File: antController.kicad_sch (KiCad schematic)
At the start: 79 parts

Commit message: work on schematic
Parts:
- removed J?: Proto_matrix, Critbit_lib:Proto_matrix_14x10, symbol Critbit_lib:Proto_matrix
- removed J?: DISP_OLED, symbol Connector_Generic:Conn_01x04
- removed J?: MOSFET_SINKS, symbol Connector:Screw_Terminal_01x16
- removed J?: OC_2, symbol Connector:Screw_Terminal_01x16
- removed JP?: 5V_SEL, symbol Jumper:SolderJumper_3_Open
- removed R? (x2): 4k7, Resistor_SMD:R_0603_1608Metric_Pad1.05x0.95mm_HandSolder, symbol Device:R
- removed R? (x2): 200, Resistor_SMD:R_0603_1608Metric_Pad1.05x0.95mm_HandSolder, symbol Device:R
- removed R? (x4): 1k, Resistor_SMD:R_0603_1608Metric_Pad1.05x0.95mm_HandSolder, symbol Device:R
- removed U?: 74LS540, symbol 74xx:74LS540
- added C? (x3): 100n, Capacitor_SMD:C_0603_1608Metric_Pad1.05x0.95mm_HandSolder, symbol Device:C_Small
- added D?: LED_RED, LED_SMD:LED_0805_2012Metric_Pad1.15x1.40mm_HandSolder, symbol Device:LED
- added J?: IO_OUT, symbol Connector_Generic:Conn_01x07
- added J? (x2): Screw_Terminal_01x20, symbol Connector:Screw_Terminal_01x20
- added J? (x3): IN_1, symbol Connector:Screw_Terminal_01x05
- added JP?: IOEX_A2_SEL, symbol Jumper:SolderJumper_3_Open
- added K?: AZ850-x, Relay_THT:Relay_DPDT_FRT5, symbol Relay:AZ850-x
- added Q? (x2): MMBT2222A, Package_TO_SOT_SMD:SOT-23, symbol Device:Q_NPN_BEC
- added R? (x7): 10k, Resistor_SMD:R_0603_1608Metric_Pad1.05x0.95mm_HandSolder, symbol Device:R
- added R? (x5): 4k7, Resistor_SMD:R_0603_1608Metric_Pad1.05x0.95mm_HandSolder, symbol Device:R
- added R?: 200k, Resistor_SMD:R_0603_1608Metric_Pad1.05x0.95mm_HandSolder, symbol Device:R
- added U? (x3): 74HC244, symbol 74xx:74HC244
- added U?: PCA9306DC, Package_SO:VSSOP-8_2.3x2mm_P0.5mm, symbol Interface:PCA9306DC
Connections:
- net +3.3V: now also C?.1, J?.2 (Pin_2), R?.2, R?.2, U?.2 (VREF1)
- net +3V3: now also C?.1, C?.1, U?.20 (VCC), U?.20 (VCC)
- net +5V: now also J?.1 (Pin_1), JP?.3 (B), K?.1, Q?.1 (B), R?.2, U?.20 (VCC)
- net BUFF1: now also J?.5 (Pin_5), U?.18 (1Y0)
- net BUFF2: now also J?.6 (Pin_6), U?.16 (1Y1)
- net BUFF3: now also J?.7 (Pin_7), U?.14 (1Y2)
- net BUFF4: now also J?.8 (Pin_8), U?.12 (1Y3)
- net BUFF5: now also J?.9 (Pin_9), U?.3 (2Y0)
- net BUFF6: now also J?.10 (Pin_10), U?.5 (2Y1)
- net BUFF7: now also J?.11 (Pin_11), U?.7 (2Y2)
- net BUFF8: now also J?.12 (Pin_12), U?.9 (2Y3)
- net GND: now also U?.2, C?.2, C?.2, C?.2, J?.13 (Pin_13), J?.19 (Pin_19), J?.2 (Pin_2), J?.20 (Pin_20), J?.3 (Pin_3), J?.4 (Pin_4), J?.5 (Pin_5), J?.5 (Pin_5), J?.5 (Pin_5), J?.7 (Pin_7), JP?.1 (A), Q?.2 (E), R?.1, R?.1, R?.1, R?.1, R?.1, R?.1, U?.1 (GND), U?.10 (GND), U?.10 (GND), U?.10 (GND); no longer R?.1, U?.3 (A2), U?.3 (A2), U?.3 (A2)
- net G_SINK1: now also R?.2; no longer Q?.1 (G)
- net IO14: now also U?.18 (1Y0)
- net IO15: now also U?.16 (1Y1)
- net IO16: now also U?.14 (1Y2)
- net IO17: now also U?.12 (1Y3)
- net IO18: now also U?.3 (2Y0)
- net IO19: now also U?.5 (2Y1)
- net IO21: now also U?.7 (2Y2)
- net IO22: now also U?.9 (2Y3)
- net IO23: now also U?.18 (1Y0)
- net IO25: now also U?.16 (1Y1)
- net IO26: now also U?.14 (1Y2)
- net IO27: now also U?.12 (1Y3)
- net IO32: now also J?.5 (Pin_5)
- net IO33: now also J?.6 (Pin_6)
- net OC1_A: now also R?.2; no longer U?.1
- net SINK1: now also J?.3 (Pin_3)
- net SINK10: now also J?.12 (Pin_12)
- net SINK11: now also J?.13 (Pin_13)
- net SINK12: now also J?.14 (Pin_14)
- net SINK13: now also J?.15 (Pin_15)
- net SINK14: now also J?.16 (Pin_16)
- net SINK15: now also J?.17 (Pin_17)
- net SINK16: now also J?.18 (Pin_18)
- net SINK2: now also J?.4 (Pin_4)
- net SINK3: now also J?.5 (Pin_5)
- net SINK4: now also J?.6 (Pin_6)
- net SINK5: now also J?.7 (Pin_7)
- net SINK6: now also J?.8 (Pin_8)
- net SINK7: now also J?.9 (Pin_9)
- net SINK8: now also J?.10 (Pin_10)
- net SINK9: now also J?.11 (Pin_11)
- net at U?.10 (IO0_6): now also U?.13 (2A2)
- net at U?.11 (IO0_7): now also U?.11 (2A3)
- net OUT_BUFF_ENA: now reaches R?.2, U?.13 (IO1_0)
- net OUT_BUFF_ENA: now also U?.1 (1OE), U?.19 (2OE)
- net IN_BUFF_ENA: now reaches U?.14 (IO1_1)
- net IN_BUFF_ENA: now also U?.1 (1OE), U?.1 (1OE), U?.19 (2OE), U?.19 (2OE)
- net at U?.18 (IO1_5): now also R?.2
- net LED1: now reaches U?.19 (IO1_6)
- net LED1: now also R?.1
- net LED2: now reaches U?.20 (IO1_7)
- net LED2: now also R?.1
- net at U?.4 (IO0_0): now also U?.2 (1A0)
- net at U?.5 (IO0_1): now also U?.4 (1A1)
- net at U?.6 (IO0_2): now also U?.6 (1A2)
- net at U?.7 (IO0_3): now also U?.8 (1A3)
- net at U?.8 (IO0_4): now also U?.17 (2A0)
- net at U?.9 (IO0_5): now also U?.15 (2A1)
- net at D?.1 (K): now also R?.2 (x6)
- net DISP_SCL: no longer names the net of U?.14 (IO12)
- net DISP_SCL: now also J?.3 (Pin_3); no longer J?.1 (Pin_1)
- net DISP_SDA: no longer names the net of U?.16 (IO13)
- net DISP_SDA: now also J?.4 (Pin_4); no longer J?.2 (Pin_2)
- net IOEX_SCL renamed SCL_5V
- net SCL_5V: now also J?.1 (Pin_1), U?.6 (SCL2); no longer U?.26 (IO4)
- net IOEX_SDA renamed SDA_5V
- net SDA_5V: now also J?.2 (Pin_2), U?.5 (SDA2); no longer U?.29 (IO5)
- net V_EXT renamed +VDC
- net +VDC: now also D?.2 (A), J?.1 (Pin_1), J?.1 (Pin_1), J?.2 (Pin_2), J?.20 (Pin_20)
- new net: JP?.2 (C), U?.3 (A2), U?.3 (A2), U?.3 (A2)
- new net: J?.14 (Pin_14), K?.2
- new net: J?.15 (Pin_15), K?.4
- new net: J?.16 (Pin_16), K?.3
- new net: J?.17 (Pin_17), K?.9
- new net: J?.18 (Pin_18), K?.7
- new net: J?.19 (Pin_19), K?.8
- new net: J?.1 (Pin_1), U?.2 (1A0) (x2)
- new net: J?.2 (Pin_2), U?.4 (1A1) (x2)
- new net: J?.3 (Pin_3), U?.6 (1A2) (x2)
- new net: J?.4 (Pin_4), U?.8 (1A3) (x2)
- new net: Q?.1 (B), R?.1
- new net: Q?.1 (G), R?.1
- new net: R?.1, U?.1
- new net: J?.4 (Pin_4), U?.11 (2A3)
- new net: J?.3 (Pin_3), U?.13 (2A2)
- new net: J?.2 (Pin_2), U?.15 (2A1)
- new net: J?.1 (Pin_1), U?.17 (2A0)
- new net: Q?.2 (E), R?.2
- new net: D?.1 (K), Q?.3 (C)
- new net: K?.10, Q?.3 (C)
- new net: R?.1, U?.7 (VREF2), U?.8 (EN)
- new net: R?.2, U?.11 (2A3), U?.13 (2A2), U?.15 (2A1), U?.17 (2A0)
- new net SCL: R?.1, U?.26 (IO4), U?.3 (SCL1)
- new net SDA: R?.1, U?.29 (IO5), U?.4 (SDA1)
- no-connect marks 24 -> 12
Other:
- note added: "TLP127?"
- note removed: "Gdzie masa na konektorach?"
- moved on the sheet: C?, D?, J?, JP?, R?, SW?, U?

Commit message: finish schematic, work on layout
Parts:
- removed C? (x2): 10u, Capacitor_SMD:C_0603_1608Metric, symbol Device:C_Small
- removed C? (x8): 100n, Capacitor_SMD:C_0603_1608Metric_Pad1.05x0.95mm_HandSolder, symbol Device:C_Small
- removed D? (x3): 1N5819WS, Diode_SMD:D_SOD-323, symbol Device:D_Schottky
- removed D?: LED, LED_SMD:LED_0805_2012Metric_Pad1.15x1.40mm_HandSolder, symbol Device:LED
- removed D? (x2): LED_RED, LED_SMD:LED_0805_2012Metric_Pad1.15x1.40mm_HandSolder, symbol Device:LED
- removed J?: IO_OUT, symbol Connector_Generic:Conn_01x07
- removed J? (x2): Screw_Terminal_01x20, symbol Connector:Screw_Terminal_01x20
- removed J? (x3): IN_1, symbol Connector:Screw_Terminal_01x05
- removed J?: OC_1, symbol Connector:Screw_Terminal_01x16
- removed J?: PWR_IN, TerminalBlock:TerminalBlock_bornier-2_P5.08mm, symbol Connector:Screw_Terminal_01x02
- removed J?: DISP_HD44780, symbol Connector_Generic:Conn_01x04
- removed J?: OC_2, symbol Connector:Screw_Terminal_01x16
- removed JP?: IOEX_A2_SEL, symbol Jumper:SolderJumper_3_Open
- removed JP?: 5V_SEL, symbol Jumper:SolderJumper_3_Open
- removed K?: AZ850-x, Relay_THT:Relay_DPDT_FRT5, symbol Relay:AZ850-x
- removed Q? (x4): MMBT2222A, Package_TO_SOT_SMD:SOT-23, symbol Device:Q_NPN_BEC
- removed Q?: BUZ11, Package_TO_SOT_THT:TO-220-3_Vertical, symbol Transistor_FET:BUZ11
- removed R? (x9): 10k, Resistor_SMD:R_0603_1608Metric_Pad1.05x0.95mm_HandSolder, symbol Device:R
- removed R? (x6): 4k7, Resistor_SMD:R_0603_1608Metric_Pad1.05x0.95mm_HandSolder, symbol Device:R
- removed R? (x4): 100k, Resistor_SMD:R_0603_1608Metric_Pad0.98x0.95mm_HandSolder, symbol Device:R_Small
- removed R?: 200k, Resistor_SMD:R_0603_1608Metric_Pad1.05x0.95mm_HandSolder, symbol Device:R
- removed U? (x3): PCA9555PW, Package_SO:TSSOP-24_4.4x7.8mm_P0.65mm, symbol Interface_Expansion:PCA9555PW
- removed U? (x2): AZ1117-ADJ, Package_TO_SOT_SMD:SOT-223-3_TabPin2, symbol Regulator_Linear:AZ1117-ADJ
- removed U? (x3): 74HC244, symbol 74xx:74HC244
- removed U?: ESP32-WROOM-32, RF_Module:ESP32-WROOM-32, symbol RF_Module:ESP32-WROOM-32
- removed U?: PCA9306DC, Package_SO:VSSOP-8_2.3x2mm_P0.5mm, symbol Interface:PCA9306DC
- removed U?: LTV-356T, Package_SO:SO-4_4.4x3.6mm_P2.54mm, symbol Isolator:LTV-356T
- added C11, C2, C4: 100n, Capacitor_SMD:C_0402_1005Metric, symbol Device:C_Small
- added C12, C5: 1n, Capacitor_SMD:C_0402_1005Metric, symbol Device:C_Small
- added C6, C7: 1n/DNP, Capacitor_SMD:C_0402_1005Metric, symbol Device:C_Small
- added J2: IDC10, Connector_IDC:IDC-Header_2x05_P2.54mm_Vertical, symbol Connector_Generic:Conn_02x05_Odd_Even
- added J3: PWRINS, TerminalBlock_MetzConnect:TerminalBlock_MetzConnect_Type055_RT01504HDWU_1x04_P5.00mm_Horizontal, symbol Connector:Screw_Terminal_01x04
- added J4: DISP_OLED, Connector_PinHeader_2.54mm:PinHeader_1x04_P2.54mm_Vertical, symbol Connector_Generic:Conn_01x04
- added J5: SMA CONN, Connector_Coaxial:SMA_Amphenol_901-143_Horizontal, symbol Connector:Conn_Coaxial
- added JP1: 5V_PROG, Jumper:SolderJumper-2_P1.3mm_Open_TrianglePad1.0x1.5mm, symbol Jumper:SolderJumper_2_Open
- added JP3: 5V_SEL, Jumper:SolderJumper-3_P2.0mm_Open_TrianglePad1.0x1.5mm, symbol Jumper:SolderJumper_3_Open
- added Q1, Q2: MMBT3904, Package_TO_SOT_SMD:SOT-23, symbol Transistor_BJT:MMBT3904
- added R10, R7, R8, R9: 4k7, Resistor_SMD:R_0402_1005Metric, symbol Device:R
- added R2: 200k, Resistor_SMD:R_0402_1005Metric, symbol Device:R
- added TP1: SMA PADS, TestPoint:TestPoint_2Pads_Pitch2.54mm_Drill0.8mm, symbol Connector:TestPoint_2Pole
- added U1: PCA9306DC, Package_SO:VSSOP-8_2.3x2mm_P0.5mm, symbol Interface:PCA9306DC
- added U2: ESP32-WROOM-32U, RF_Module:ESP32-WROOM-32U, symbol RF_Module:ESP32-WROOM-32U
- added U3: AZ1117-3.3, Package_TO_SOT_SMD:SOT-223-3_TabPin2, symbol Regulator_Linear:AZ1117-3.3
- C1: renamed from C?; footprint Capacitor_SMD:C_1206_3216Metric_Pad1.42x1.75mm_HandSolder -> Capacitor_SMD:C_0603_1608Metric
- C13, C14, C3, C8: renamed from C?; footprint Capacitor_SMD:C_0603_1608Metric_Pad1.05x0.95mm_HandSolder -> Capacitor_SMD:C_0402_1005Metric
- D1, D2, D4: renamed from D?; footprint LED_SMD:LED_0805_2012Metric_Pad1.15x1.40mm_HandSolder -> LED_THT:LED_D3.0mm
- D3: renamed from D?; value LED -> LED_RED; footprint LED_SMD:LED_0805_2012Metric_Pad1.15x1.40mm_HandSolder -> LED_THT:LED_D3.0mm
- J1: renamed from J?; footprint Critbit_lib:Lichtenprog -> Critbit_lib:Lichtenprog_board
- JP2: renamed from JP?; value 5V_SEL -> 3V3_SEL; footprint (none) -> Jumper:SolderJumper-3_P2.0mm_Open_TrianglePad1.0x1.5mm
- R11, R12, R3, R4, R5: renamed from R?; footprint Resistor_SMD:R_0603_1608Metric_Pad1.05x0.95mm_HandSolder -> Resistor_SMD:R_0402_1005Metric
- R13: renamed from R?; value 10k -> 33k; footprint Resistor_SMD:R_0603_1608Metric_Pad1.05x0.95mm_HandSolder -> Resistor_SMD:R_0402_1005Metric
- R14, R15: renamed from R?; value 10k -> 15k; footprint Resistor_SMD:R_0603_1608Metric_Pad1.05x0.95mm_HandSolder -> Resistor_SMD:R_0402_1005Metric
- R16: renamed from R?; value 100k -> 240; footprint Resistor_SMD:R_0603_1608Metric_Pad0.98x0.95mm_HandSolder -> Resistor_SMD:R_0402_1005Metric
- R17: renamed from R?; value 100k -> 720; footprint Resistor_SMD:R_0603_1608Metric_Pad0.98x0.95mm_HandSolder -> Resistor_SMD:R_0402_1005Metric
- R18: renamed from R?; value 4k7 -> 100k; footprint Resistor_SMD:R_0603_1608Metric_Pad1.05x0.95mm_HandSolder -> Resistor_SMD:R_0402_1005Metric
- gave numbers to parts that had none: 9
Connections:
- net +3V3 is gone; now on net +3.3V: JP2.2 (C)
- net +3.3V: now also C2.1, J4.3 (Pin_3), R7.2, R8.2, U1.2 (VREF1), U2.2 (VDD)
- net +5V: now also C9.1, D1.2 (A), JP3.2 (C), R10.2, R2.2, R9.2
- net +VDC: now also C11.1, C12.1, J3.2 (Pin_2)
- net B2: now also U2.7 (IO35)
- net B3: now also U2.6 (IO34)
- net ESP_BOOT: now also Q2.3 (C), U2.25 (IO0)
- net ESP_EN: now also Q1.3 (C), U2.3 (EN)
- net GND: now also C11.2, C12.2, C2.2, C4.2, C5.2, C6.2, C7.2, J2.7 (Pin_7), J2.8 (Pin_8), J3.1 (Pin_1), J3.3 (Pin_3), J4.4 (Pin_4), J5.2 (Ext), TP1.1, U1.1 (GND), U2.1 (GND), U2.15 (GND), U2.38 (GND), U2.39 (GND), U3.1 (GND)
- net IN_BUFF_ENA: now also U2.16 (IO13)
- net IO14: now also U2.13 (IO14)
- net IO15: now also U2.23 (IO15)
- net IO16: now also U2.27 (IO16)
- net IO17: now also U2.28 (IO17)
- net IO18: now also U2.30 (IO18)
- net IO19: now also U2.31 (IO19)
- net IO21: now also U2.33 (IO21)
- net IO22: now also U2.36 (IO22)
- net IO23: now also U2.37 (IO23)
- net IO25: now also U2.10 (IO25)
- net IO26: now also U2.11 (IO26)
- net IO27: now also U2.12 (IO27)
- net PROG_3V3: now also J2.1 (Pin_1), J2.2 (Pin_2)
- net PROG_5V: now also C4.1, C5.1, J2.10 (Pin_10), J2.9 (Pin_9), JP1.1 (A)
- net PROG_DTR: now also J2.6 (Pin_6), Q2.2 (E)
- net PROG_RTS: now also J2.4 (Pin_4), Q1.2 (E)
- net RXD: now also J2.3 (Pin_3), U2.34 (RXD0/IO3)
- net SCL: now also C6.1, J4.2 (Pin_2), R7.1, U1.3 (SCL1), U2.26 (IO4)
- net SCL_5V: now also R9.1, U1.6 (SCL2)
- net SDA: now also C7.1, J4.1 (Pin_1), R8.1, U1.4 (SDA1), U2.29 (IO5)
- net SDA_5V: now also R10.1, U1.5 (SDA2)
- net TXD: now also J2.5 (Pin_5), U2.35 (TXD0/IO1)
- net at R16.1, U4.2 (VO): now also JP3.1 (A)
- net at R18.2: now also D4.1 (K)
- net at R1.2: now also Q1.1 (B)
- net at R3.1: now also U2.24 (IO2)
- net at R6.2: now also Q2.1 (B)
- net LED1 renamed LED_STATUS
- net LED_STATUS: now also U2.9 (IO33)
- new net: R2.1, U1.7 (VREF2), U1.8 (EN)
- new net: J3.4 (Pin_4), JP1.2 (B), JP3.3 (B)
- new net: J5.1 (In), TP1.2
- new net I2C_RST: U2.14 (IO12)
- new net OUT_BUF_ENA: U2.8 (IO32)
- no-connect marks 12 -> 8
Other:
- added sheet Back connectors (back_connectors.kicad_sch)
- note added: "5V"
- note added: "5V out"
- note added: "7V - 37V"
- note added: "@12V: dV=7V, P=1,2*7=8.4W @24V: dV=19V P=0,74*19=22.8W"
- note added: "For 5V: Idc max = ~100mA + 16x relay@40mA + 400mA@3V3 =~ 1.2A"
- note added: "Idc max ~400mA"
- note added: "Target LED current ~0.1mA dU = 1.9 3V3 - 15k 5V - 33k 13.8V - 120k"
- note added: "Wymagania 15. Oszacuj pobór prądów 3,3/5V, w razie czego miejsce na radiatory dla stabilizatorów. Policzyć rezystory. 2. BUZ11 TO220, dren w środku 4. drugi PCA steruje 16-toma przekaźnikami (wg. pin-outu przesłanego) poprzez tranzystory bipolarne 5. trzeci PCA dolna ósemka - transoptory, rezystor szeregowy diody 4k7 6. 12 wejść zabezpieczyc filtrem RF R=10k + C=10nF Gniazda DB25 na jednaj krawęd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"
- note removed: "12V out"
- note removed: "15V max"
- note removed: "TLP127?"
- moved on the sheet: C1, C10, C13, C14, C3, C8, C9, D1, D2, D3, D4, J1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

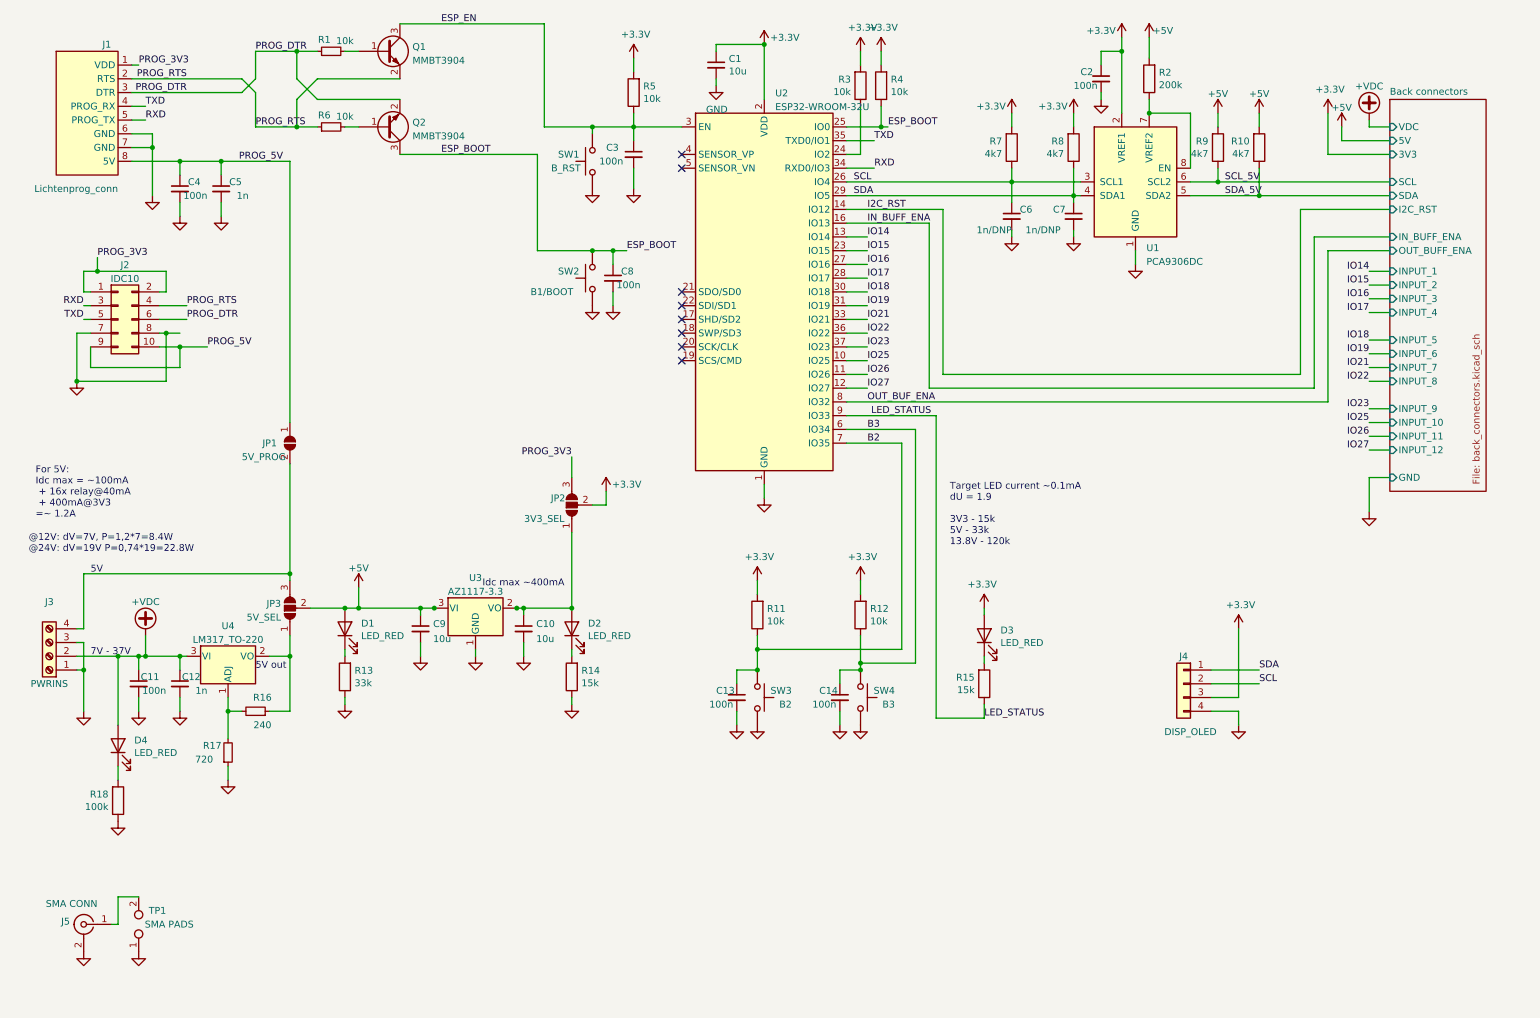
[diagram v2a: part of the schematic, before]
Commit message: routing mostly done, fixing schematic issues
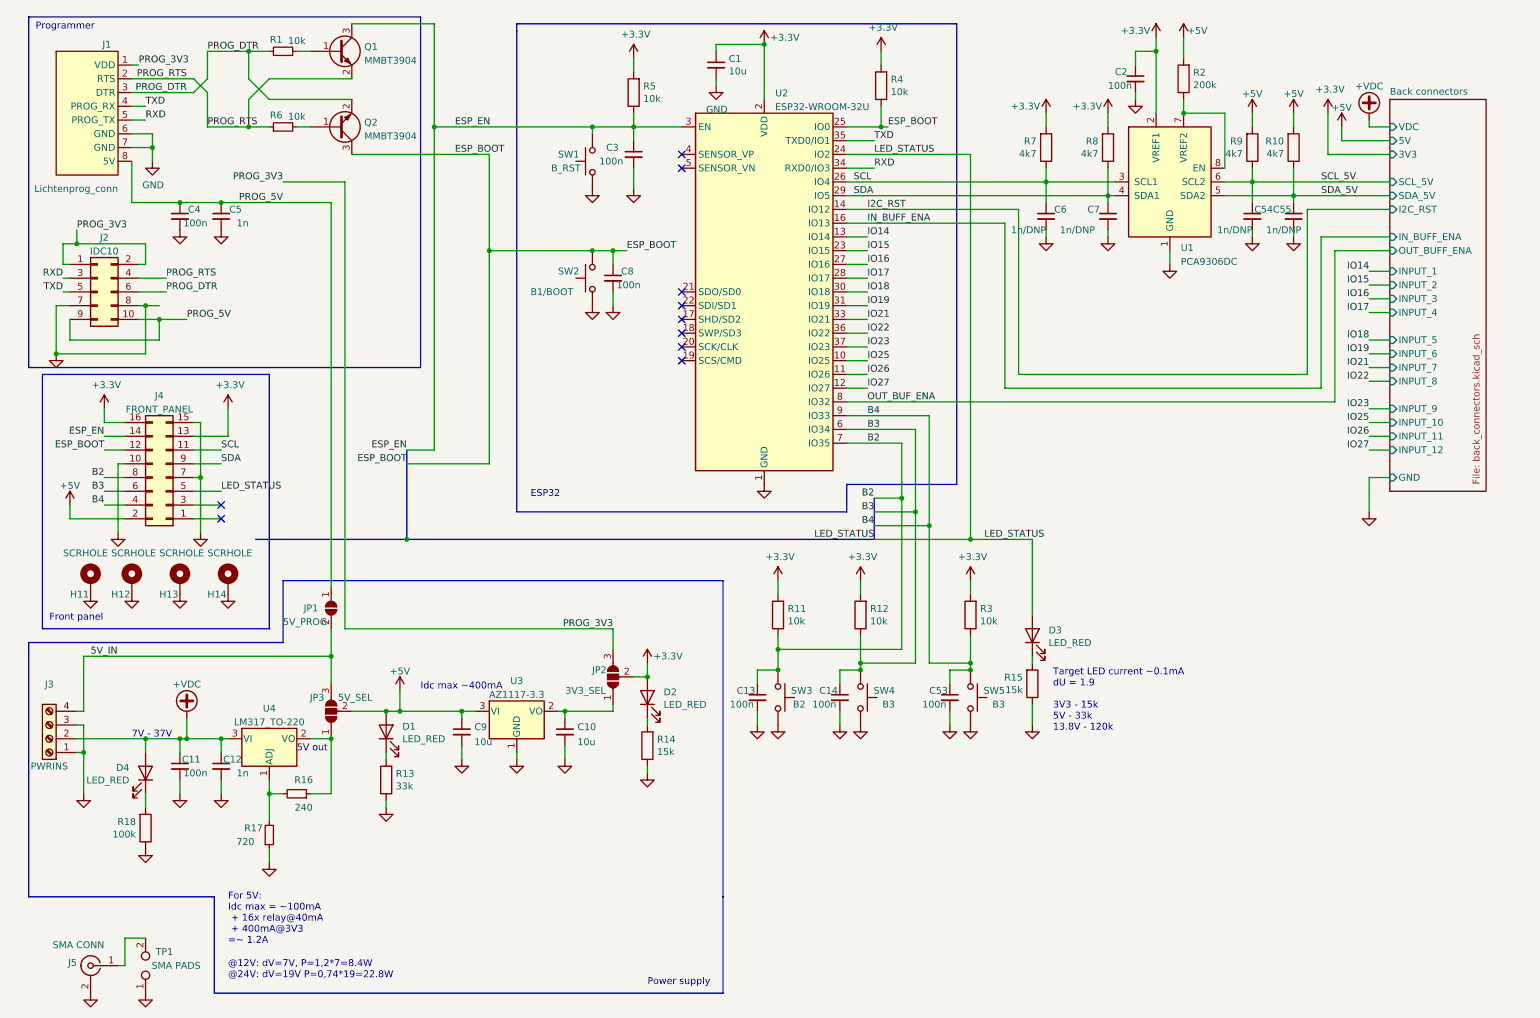
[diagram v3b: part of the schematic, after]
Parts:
- removed J4: DISP_OLED, Connector_PinHeader_2.54mm:PinHeader_1x04_P2.54mm_Vertical, symbol Connector_Generic:Conn_01x04
- added C53: 100n, Capacitor_SMD:C_0402_1005Metric, symbol Device:C_Small
- added C54, C55: 1n/DNP, Capacitor_SMD:C_0402_1005Metric, symbol Device:C_Small
- added H11, H12, H13, H14: SCRHOLE, MountingHole:MountingHole_3.2mm_M3_ISO7380_Pad, symbol Mechanical:MountingHole_Pad
- added J4: FRONT_PANEL, Connector_PinHeader_2.54mm:PinHeader_2x08_P2.54mm_Horizontal, symbol Connector_Generic:Conn_02x08_Odd_Even
- added SW5: B3, Button_Switch_SMD:SW_SPST_TL3342, symbol Switch:SW_Push
- D1, D2, D3, D4: footprint LED_THT:LED_D3.0mm -> LED_SMD:LED_0603_1608Metric
- SW1, SW2, SW3, SW4: footprint Button_Switch_THT:SW_Tactile_SPST_Angled_PTS645Vx83-2LFS -> Button_Switch_SMD:SW_SPST_TL3342
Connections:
- net +3.3V: now also D2.2 (A), J4.13 (Pin_13), J4.16 (Pin_16); no longer D3.2 (A)
- net +5V: now also U3.3 (VI), J4.2 (Pin_2)
- net B2: now also J4.8 (Pin_8)
- net B3: now also J4.6 (Pin_6)
- net ESP_BOOT: now also J4.12 (Pin_12)
- net ESP_EN: now also J4.14 (Pin_14)
- net GND: now also R15.1, C53.2, C54.2, C55.2, H11.1, H12.1, H13.1, H14.1, J4.10 (Pin_10), J4.15 (Pin_15), J4.7 (Pin_7), SW5.1
- net LED_STATUS: now also D3.2 (A), U2.24 (IO2), J4.5 (Pin_5); no longer R15.1, U2.9 (IO33)
- net SCL: now also J4.11 (Pin_11)
- net SCL_5V: now also C54.1
- net SDA: now also J4.9 (Pin_9)
- net SDA_5V: now also C55.1
- net at U3.2 (VO): now also C10.1, JP2.1 (A)
- net 5V_IN: now reaches J3.4 (Pin_4), JP1.2 (B), JP3.3 (B)
- net B4: now reaches R3.1
- net B4: now also U2.9 (IO33), C53.1, J4.4 (Pin_4), SW5.2; no longer U2.24 (IO2)
- no-connect marks 8 -> 10
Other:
- sheet Back connectors ports: added SCL_5V, SDA_5V; removed SCL, SDA
- note added: "ESP32"
- note added: "Front panel"
- note added: "Power supply"
- note added: "Programmer"
- note removed: "5V"
- moved on the sheet: C10, C11, C12, C13, C2, C4, C5, C6, C7, C9, D1, D2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
